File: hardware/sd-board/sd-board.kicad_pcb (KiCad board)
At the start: 2 copper layers, 25.4 x 78.2 mm, 10 parts, among them J1 TF-01A push-push, J2 FPC 10P 0.5mm (IN), J3 FPC 10P 0.5mm (LCD), U1 74LVC1G04

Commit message: feat(hardware): J2 5 mm lower (57 mm up, 1 mm right) for the 80 mm cable from J12 (the user); the LCD cable reaches J3, tested by the user; DRC 0, nets 0 differ
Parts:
- moved J2 5.10 mm to (192.4, 143.0)
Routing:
- net LCD_RST: track 17.5 -> 23.5 mm
- net LCD_LEDK: track 17.5 -> 23.5 mm
- net LCD_LEDA: track 17.5 -> 23.5 mm
- net MOSI: track 75.9 -> 76.7 mm
- net LCD_CS: track 64.2 -> 65.0 mm
- net CLK: track 77.2 -> 78.0 mm
- net 3V3: track 107.3 -> 108.1 mm
- net MISO: track 72.4 -> 73.2 mm

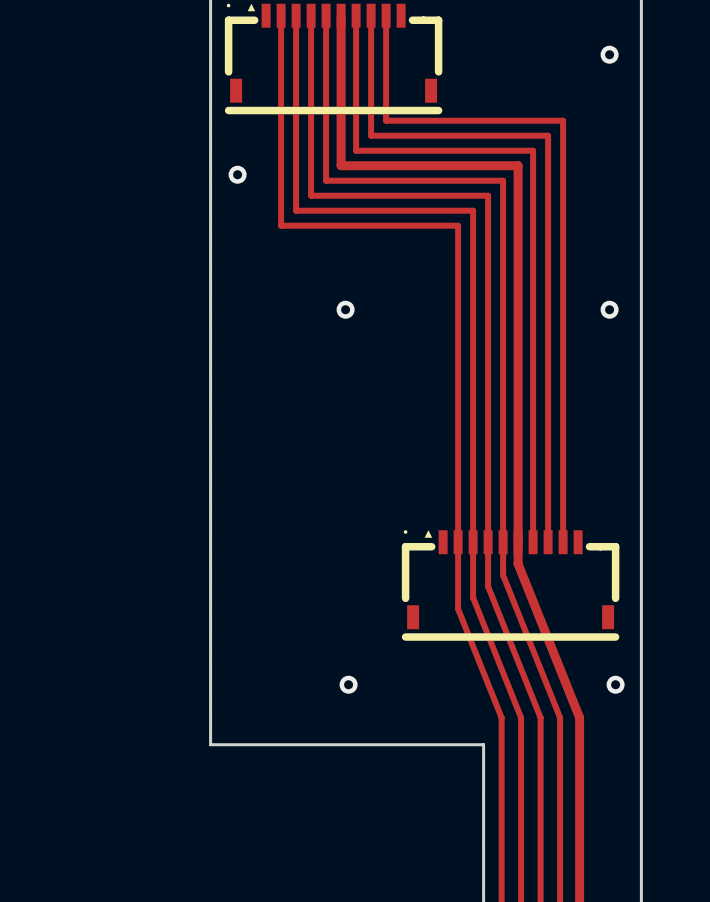
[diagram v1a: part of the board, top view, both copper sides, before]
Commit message: feat(hardware): R1 220 ohm (C22962: the card reads at 20 MHz, the firmware keeps D/C high at idle), silkscreen 'LCD: gold UP' / 'IN: gold DOWN' (the double-sided sockets connect a turned-over cable mirrored); the 33 ohm and ESD parts listed for the re-route after the pin map
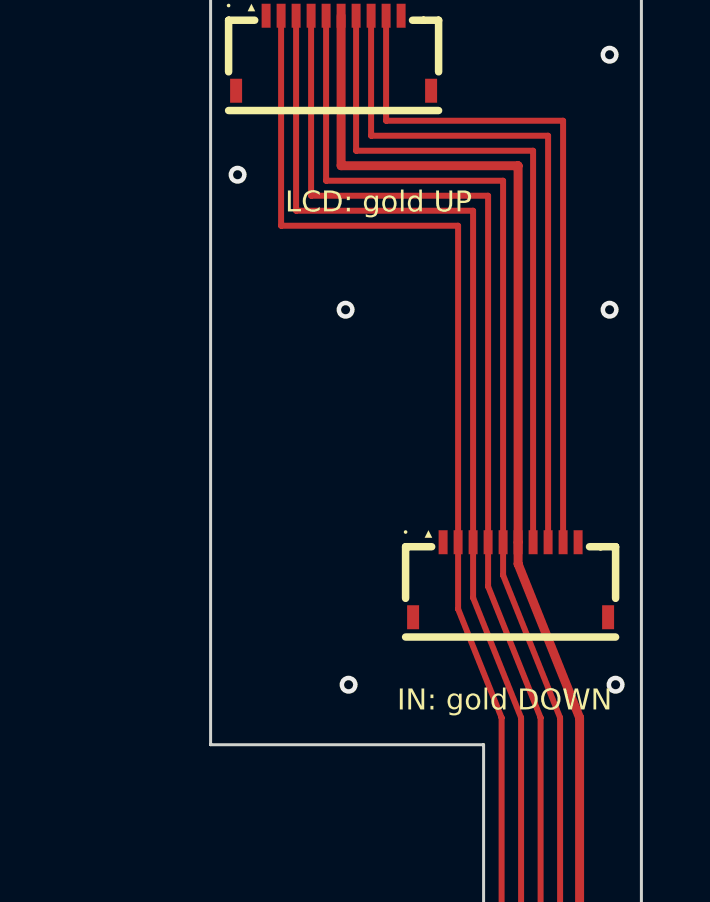
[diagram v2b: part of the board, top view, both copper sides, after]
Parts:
- R1: value 1k -> 220
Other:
- board text added: "IN: gold DOWN"
- board text added: "LCD: gold UP"

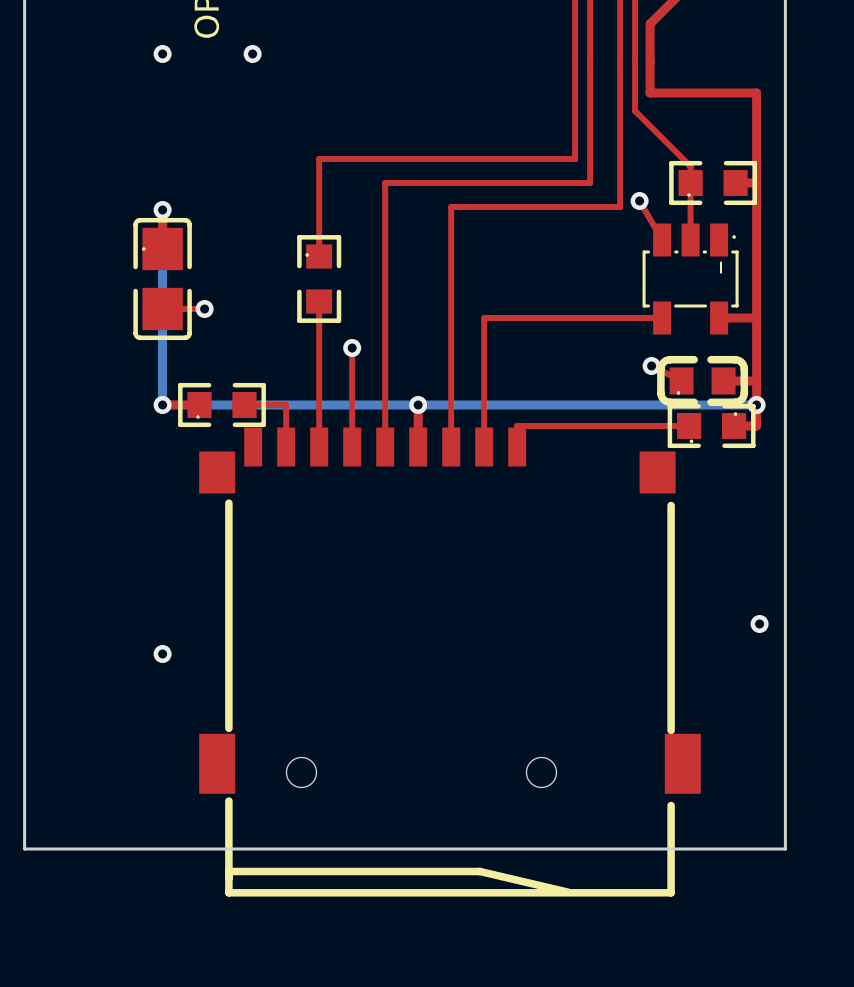
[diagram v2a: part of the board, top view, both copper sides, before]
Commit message: feat(hardware): the card socket 1 mm further out, the card 1 mm past the case's outside (the user); DRC 0, nets 0 differ
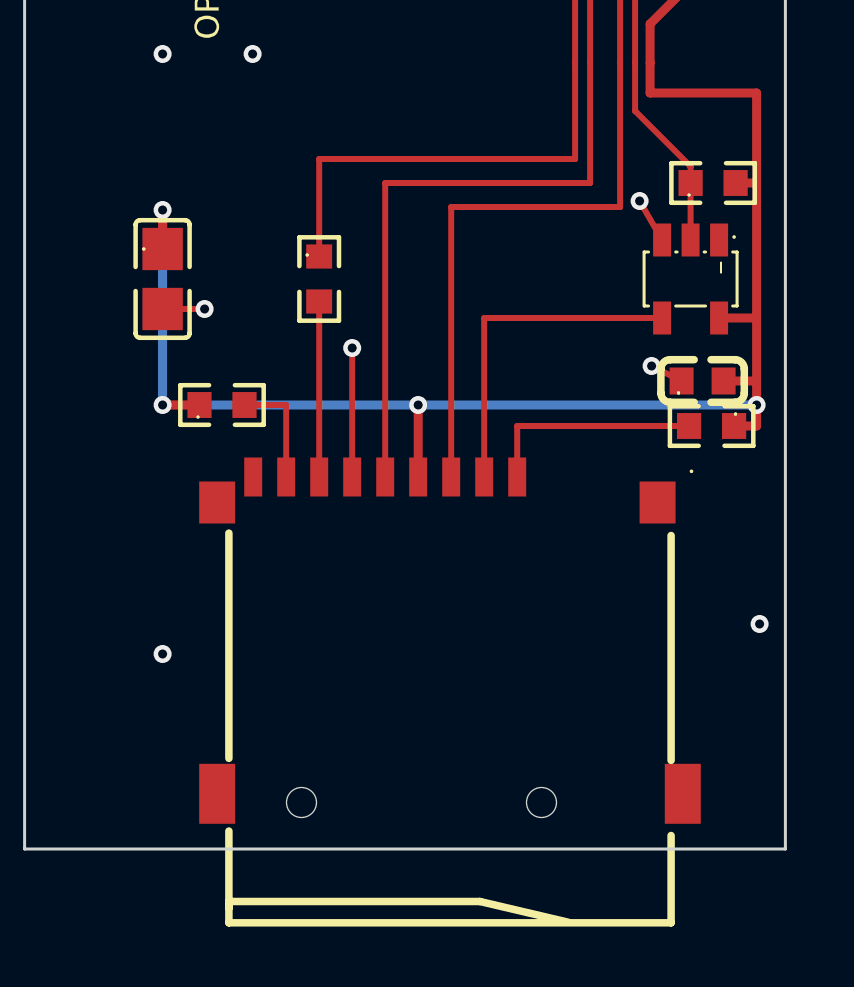
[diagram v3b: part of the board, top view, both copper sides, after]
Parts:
- moved J1 1.00 mm to (185.6, 194.4)
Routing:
- net GND: track 7.32 -> 8.32 mm
- net MOSI: track 76.7 -> 77.7 mm
- net DAT2: track 6.43 -> 7.43 mm
- net DAT1: track 2.79 -> 3.79 mm
- net DAT0: track 4.85 -> 5.85 mm
- net CLK: track 78.0 -> 79.0 mm
- net CARD_CS: track 10.2 -> 11.2 mm
- net 3V3: track 108.1 -> 109.1 mm

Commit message: feat(hardware): the card 0.5 mm past the case's outside (the user)
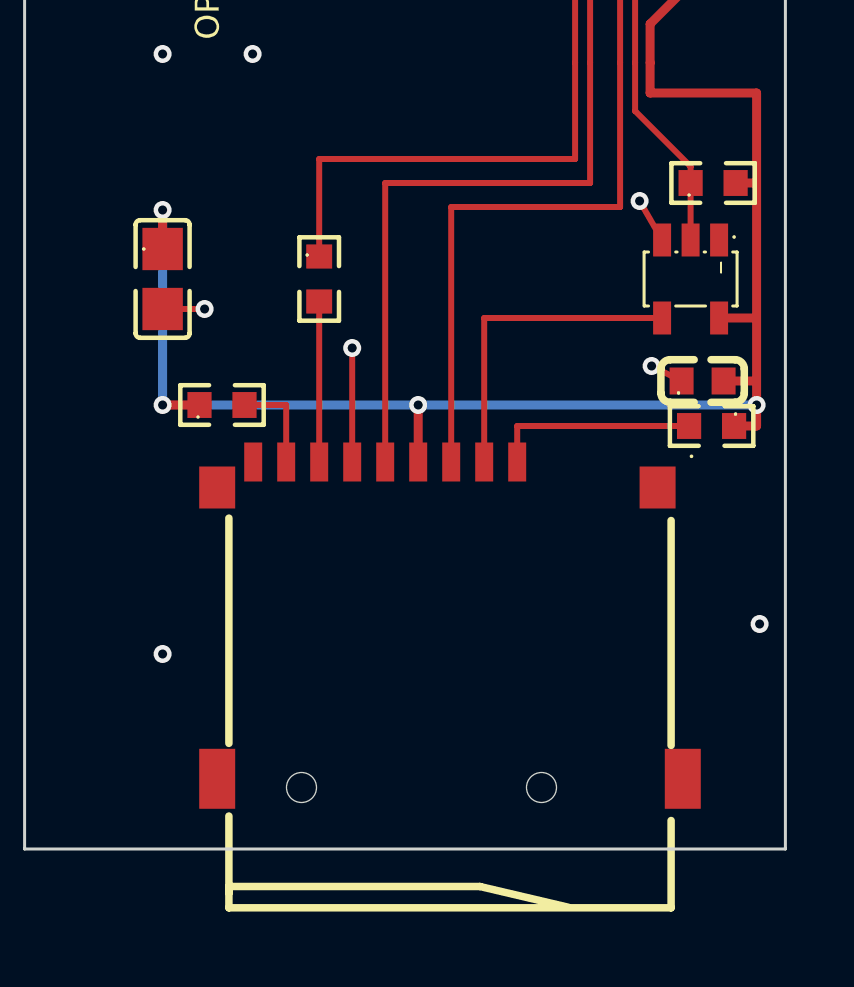
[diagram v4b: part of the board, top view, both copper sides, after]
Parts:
- moved J1 0.50 mm to (185.6, 193.9)
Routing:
- net GND: track 8.32 -> 7.82 mm
- net MOSI: track 77.7 -> 77.2 mm
- net DAT2: track 7.43 -> 6.93 mm
- net DAT1: track 3.79 -> 3.29 mm
- net DAT0: track 5.85 -> 5.35 mm
- net CLK: track 79.0 -> 78.5 mm
- net CARD_CS: track 11.2 -> 10.7 mm
- net 3V3: track 109.1 -> 108.6 mm

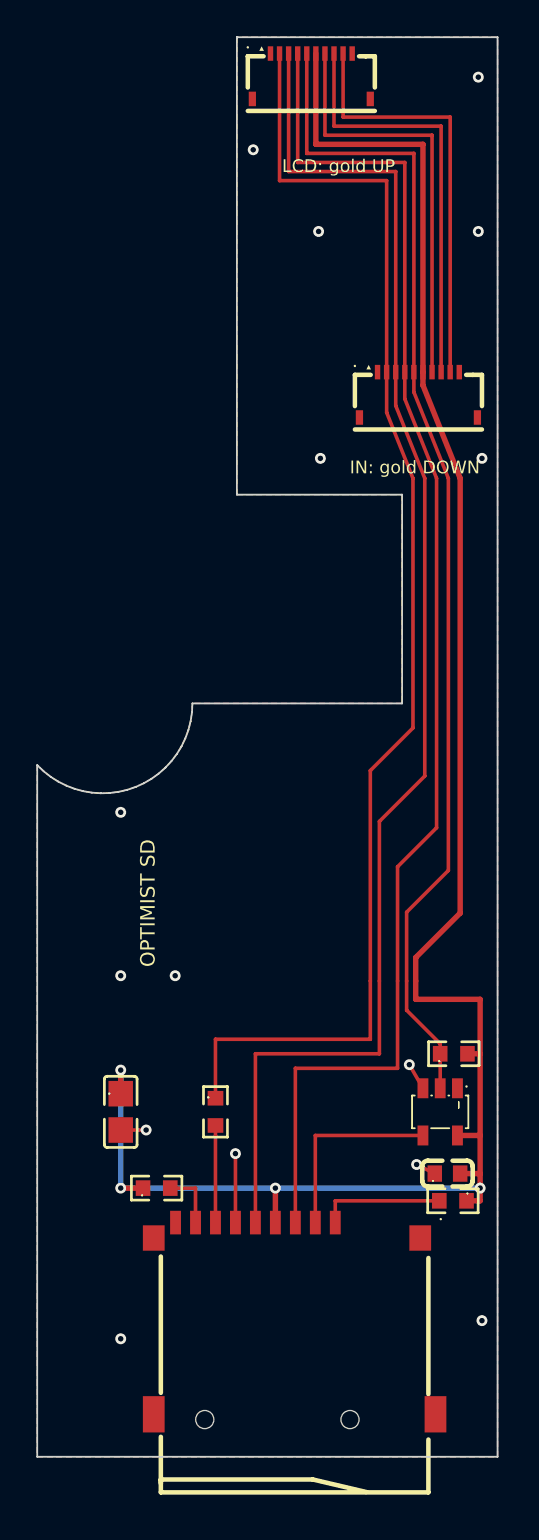
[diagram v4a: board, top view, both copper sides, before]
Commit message: feat(sd-board): v6, rerouted to J12's probed pin map (2 PC8, 3 PC7 CS, 4 PC9 CLK, 5 PC10 MOSI, 7 3.3 V to confirm): J3 single-sided top contact (C3446068, wired by place), R4 a pull-down, R1/R5/R6 100 ohm (R5, R6 in series on CLK and MOSI at the column's top), the column in J2's order with a ground guard lane between CS and CLK, CS across on the bottom, U1/R2/R4/C2 off the tray's lips (asserted); DRC 0, nets 48 = 48. Not ready to order: pin 7, the mirror check (J2's face), the ESD (USBLC6-2SC6 is two lines: USBLC6-4SC6 not placed yet)
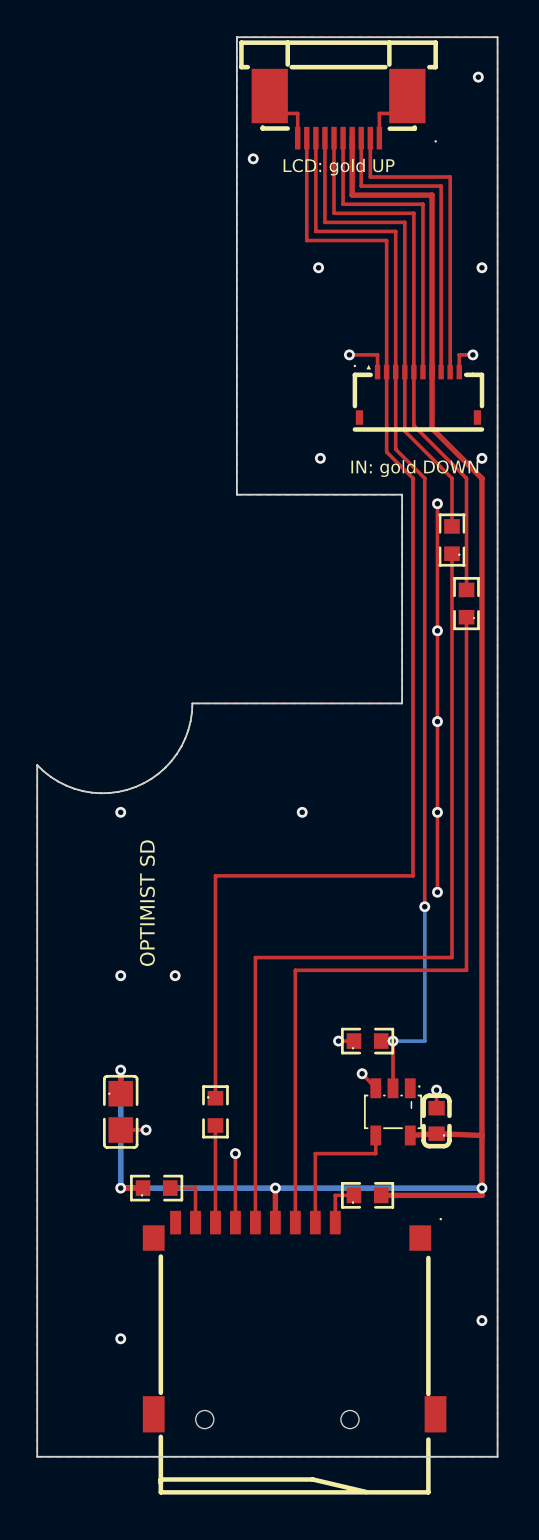
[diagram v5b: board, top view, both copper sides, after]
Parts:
- added R5: 100, sdboard:R0603, F.Cu at (194.2, 151.0)
- added R6: 100, sdboard:R0603, F.Cu at (195.1, 154.5)
- J3: value FPC 10P 0.5mm (LCD) -> FPC 10P 0.5mm top contact (LCD); footprint sdboard:FPC-SMD_10P-P0.50_HC-FPC-05-09-10RLTAG -> sdboard:FPC-SMD_10P-P0.50_XUNPU_FPC-0.5AS-10PWBH20
- R1: value 220 -> 100
- moved R4 4.80 mm to (189.6, 178.6)
- moved R2 4.71 mm to (189.6, 187.1), turned to 0 degrees
- moved C2 2.96 mm to (193.4, 183.0), turned to 90 degrees
- moved J3 2.70 mm to (188.0, 127.7)
- moved U1 2.60 mm to (191.0, 182.5)
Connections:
- C2 pad 1: GND -> 3V3
- C2 pad 2: 3V3 -> GND
- J1 pad 3: MOSI -> MOSI_SD
- J1 pad 5: CLK -> CLK_SD
- J2 pad 3: CLK -> LCD_CS
- J2 pad 4: MOSI -> CLK
- J2 pad 5: LCD_CS -> MOSI
- J2 pad 6: 3V3 -> LCD_6
- J2 pad 7: LCD_RST -> 3V3
- J2 pad 8: LCD_LEDA -> LCD_8
- J2 pad 9: LCD_LEDK -> LCD_9
- J3 pad 2: MISO -> LCD_9
- J3 pad 3: CLK -> LCD_8
- J3 pad 4: MOSI -> 3V3
- J3 pad 5: LCD_CS -> LCD_6
- J3 pad 6: 3V3 -> MOSI
- J3 pad 7: LCD_RST -> CLK
- J3 pad 8: LCD_LEDA -> LCD_CS
- J3 pad 9: LCD_LEDK -> MISO
- R2 pad 1: 3V3 -> DAT2
- R2 pad 2: DAT2 -> 3V3
- R4 pad 1: LCD_CS -> GND
- R4 pad 2: 3V3 -> LCD_CS
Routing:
- net CLK: track 78.5 -> 26.9 mm
- net CLK_SD: track 0.00 -> 47.7 mm
- net MOSI: track 77.2 -> 30.5 mm
- net MOSI_SD: track 0.00 -> 42.8 mm
- net GND: track 7.82 -> 39.5 mm, vias 15 -> 24
- net LCD_RST: track 23.5 -> 0.00 mm
- net LCD_LEDK: track 23.5 -> 0.00 mm
- net LCD_LEDA: track 23.5 -> 0.00 mm
- net LCD_9: track 0.00 -> 17.3 mm
- net LCD_8: track 0.00 -> 17.3 mm
- net LCD_6: track 0.00 -> 17.3 mm
- net LCD_CS: track 65.0 -> 59.8 mm, vias 0 -> 2
- net 3V3: track 108.6 -> 104.1 mm
- net MISO: track 73.2 -> 68.8 mm
- net DAT2: track 6.93 -> 2.53 mm
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
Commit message: feat(sd-board): ESD (two USBLC6-2SC6, C7519, every card line straight through a column: no stub), the swap block (Julius's idea: each line DO, CS, CLK, DI, 3V3 through a bridged solder jumper between J2 and the SD part: cut and wire to fix a wrong J12 guess) and test pads on J12's unprobed pins 6, 8, 9 and GND; DRC 0, nets 74 = 74; READMEs: the ESD is no longer open
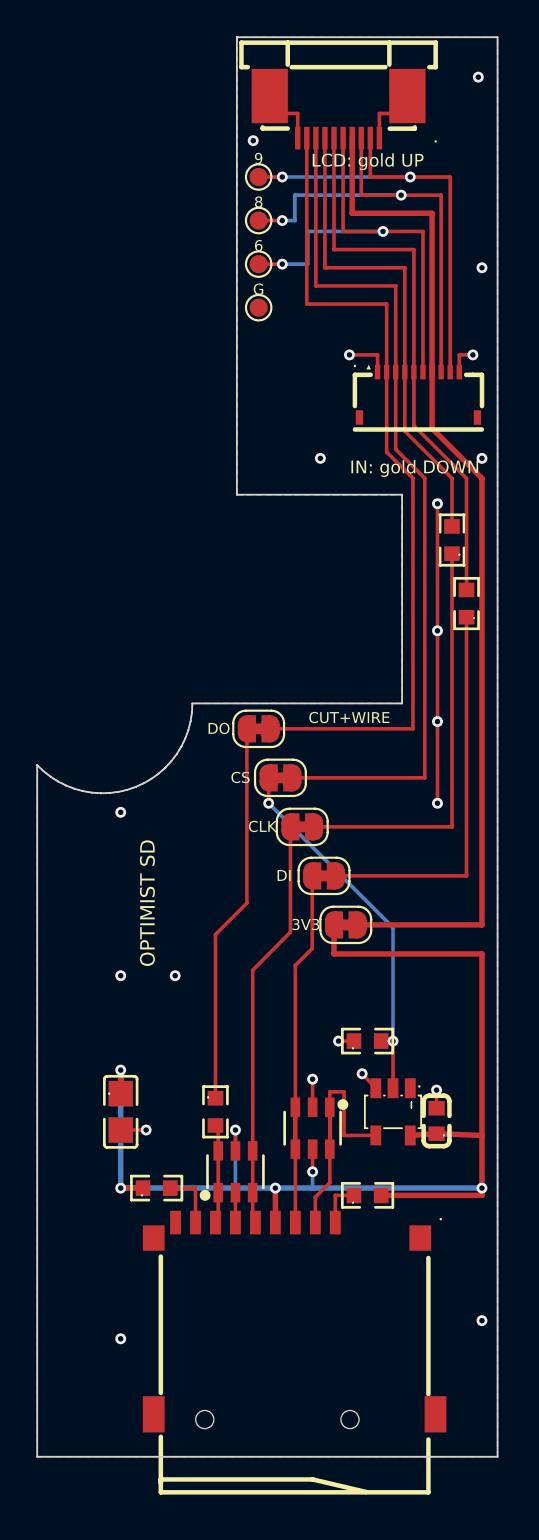
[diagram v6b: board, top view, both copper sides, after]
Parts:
- added JP1: cut to swap, Jumper:SolderJumper-2_P1.3mm_Bridged_RoundedPad1.0x1.5mm, F.Cu at (183.6, 161.4)
- added JP2: cut to swap, Jumper:SolderJumper-2_P1.3mm_Bridged_RoundedPad1.0x1.5mm, F.Cu at (184.8, 164.1)
- added JP3: cut to swap, Jumper:SolderJumper-2_P1.3mm_Bridged_RoundedPad1.0x1.5mm, F.Cu at (186.0, 166.8)
- added JP4: cut to swap, Jumper:SolderJumper-2_P1.3mm_Bridged_RoundedPad1.0x1.5mm, F.Cu at (187.2, 169.5)
- added JP5: cut to swap, Jumper:SolderJumper-2_P1.3mm_Bridged_RoundedPad1.0x1.5mm, F.Cu at (188.4, 172.2)
- added TP1: J12 6, TestPoint:TestPoint_Pad_D1.0mm, F.Cu at (183.6, 135.8)
- added TP2: J12 8, TestPoint:TestPoint_Pad_D1.0mm, F.Cu at (183.6, 133.4)
- added TP3: J12 9, TestPoint:TestPoint_Pad_D1.0mm, F.Cu at (183.6, 131.0)
- added TP4: J12 G, TestPoint:TestPoint_Pad_D1.0mm, F.Cu at (183.6, 138.2)
- added U2: USBLC6-2SC6, sdboard:SOT-23-6_L2.9-W1.6-P0.95-LS2.8-BL, F.Cu at (186.6, 183.4)
- added U3: USBLC6-2SC6, sdboard:SOT-23-6_L2.9-W1.6-P0.95-LS2.8-BL, F.Cu at (182.3, 185.8)
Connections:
- C1 pad 1: 3V3 -> SD_VDD
- C2 pad 1: 3V3 -> SD_VDD
- J1 pad 3: MOSI_SD -> SD_DI
- J1 pad 4: 3V3 -> SD_VDD
- J1 pad 5: CLK_SD -> SD_CLK
- R1 pad 1: MISO -> SD_DO
- R2 pad 2: 3V3 -> SD_VDD
- R3 pad 1: 3V3 -> SD_VDD
- R4 pad 2: LCD_CS -> SD_CSIN
- U1 pad 2: LCD_CS -> SD_CSIN
- U1 pad 5: 3V3 -> SD_VDD
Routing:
- net SD_VDD: track 0.00 -> 69.9 mm, vias 0 -> 6
- net 3V3: track 104.1 -> 55.7 mm, vias 4 -> 0
- net CLK_SD: track 47.7 -> 22.7 mm
- net SD_DI: track 0.00 -> 24.1 mm
- net MISO: track 68.8 -> 45.4 mm
- net SD_CLK: track 0.00 -> 22.7 mm
- net MOSI_SD: track 42.8 -> 21.5 mm
- net SD_DO: track 0.00 -> 21.1 mm
- net SD_CSIN: track 0.00 -> 20.6 mm, vias 0 -> 2
- net LCD_CS: track 59.8 -> 47.6 mm, vias 2 -> 0
- net LCD_8: track 17.3 -> 26.5 mm, vias 0 -> 2
- net CARD_CS: track 8.13 -> 17.1 mm
- net LCD_6: track 17.3 -> 25.9 mm, vias 0 -> 2
- net LCD_9: track 17.3 -> 25.6 mm, vias 0 -> 2
- net GND: track 39.5 -> 34.0 mm, vias 24 -> 21
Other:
- board text added: "3V3"
- board text added: "6"
- board text added: "8"
- board text added: "9"
- board text added: "CLK"
- board text added: "CS"
- board text added: "CUT+WIRE"
- board text added: "DI"
- board text added: "DO"
- board text added: "G"

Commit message: feat(sd-board): the swap jumpers bigger (own footprint: 1.5 x 2 mm pads 3 mm apart, a 1.5 mm bare bridge to cut), J12's pin number right of each J12-side pad, the test pads 1.5 mm; DRC 0, nets 74 = 74
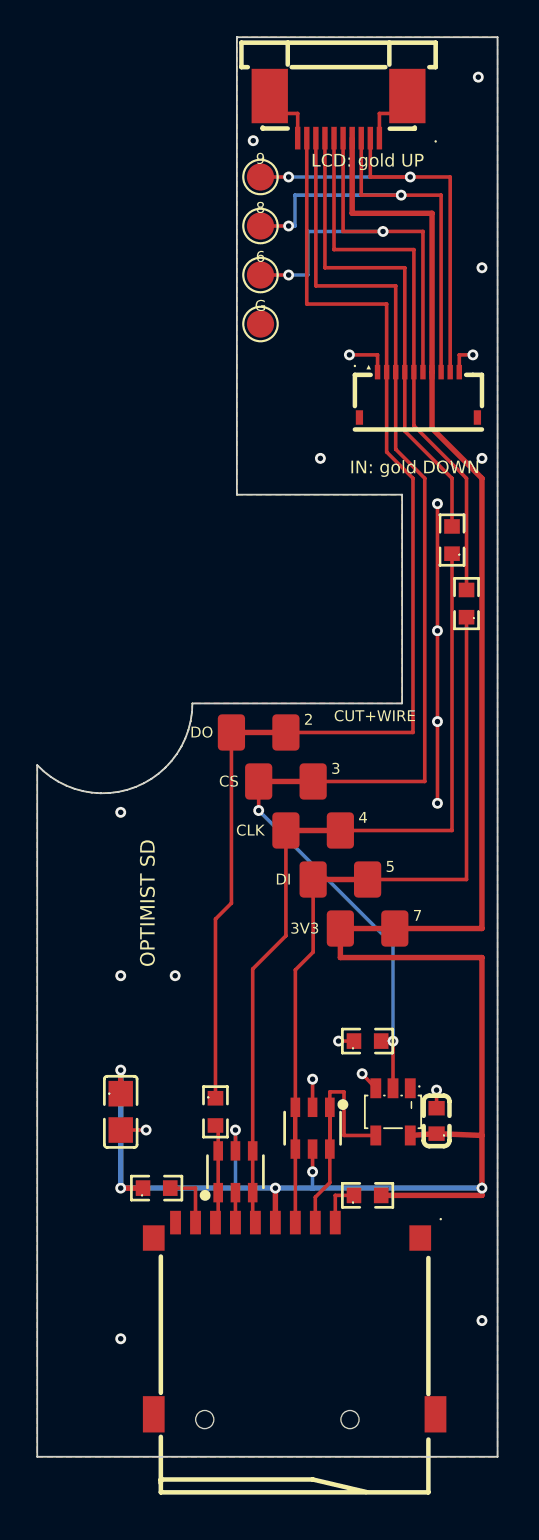
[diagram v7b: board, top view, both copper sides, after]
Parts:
- JP1, JP2, JP3, JP4, JP5: footprint Jumper:SolderJumper-2_P1.3mm_Bridged_RoundedPad1.0x1.5mm -> sdboard:SolderJumper-2_Cut_P3.0mm_Pad1.5x2.0mm
- TP1, TP2, TP3, TP4: footprint TestPoint:TestPoint_Pad_D1.0mm -> TestPoint:TestPoint_Pad_D1.5mm
- moved JP5 1.22 mm to (189.6, 172.4)
- moved JP4 0.92 mm to (188.1, 169.7)
- moved TP4 0.91 mm to (183.7, 139.1)
- moved JP3 0.63 mm to (186.6, 167.0)
- moved TP1 0.61 mm to (183.7, 136.4)
- moved JP2 0.36 mm to (185.1, 164.3)
- moved TP2 0.32 mm to (183.7, 133.7)
- moved JP1 0.20 mm to (183.6, 161.6)
- moved TP3 0.10 mm to (183.7, 131.0)
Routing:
- net 3V3: track 55.7 -> 53.9 mm
- net MOSI_SD: track 21.5 -> 19.9 mm
- net CLK_SD: track 22.7 -> 21.4 mm
- net LCD_CS: track 47.6 -> 46.7 mm
- net MISO: track 45.4 -> 44.7 mm
- net SD_DO: track 21.1 -> 20.5 mm
- net SD_VDD: track 69.9 -> 69.3 mm
- net LCD_6: track 25.9 -> 26.4 mm
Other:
- board text added: "2"
- board text added: "3"
- board text added: "4"
- board text added: "5"
- board text added: "7"
